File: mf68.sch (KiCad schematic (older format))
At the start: 2 parts, among them SW1 MX, U1 nice_nano

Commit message: Start working on matrix
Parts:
- removed SW1: MX, Keebio-Parts:MX-Alps-Choc-1U, symbol keebio:MX
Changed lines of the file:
@@
 $Descr A4 11693 8268
 encoding utf-8
-Sheet 1 1
+Sheet 1 2
 Title ""
 Date ""
@@
 	1    0    0    -1
 $EndComp
-$Comp
-L keebio:MX SW1
-U 1 1 6192757C
-P 3650 2550
-F 0 "SW1" H 3650 2773 50  0000 C CNN
-F 1 "MX" H 3650 2250 60  0001 C CNN
-F 2 "Keebio-Parts:MX-Alps-Choc-1U" H 3650 2550 60  0001 C CNN
-F 3 "" H 3650 2550 60  0001 C CNN
-	1    3650 2550
-	1    0    0    -1
-$EndComp
+$Sheet
+S 3950 2050 2750 1350
+U 6194AF7C
+F0 "matrix" 50
+F1 "matrix.sch" 50
+$EndSheet
 $EndSCHEMATC

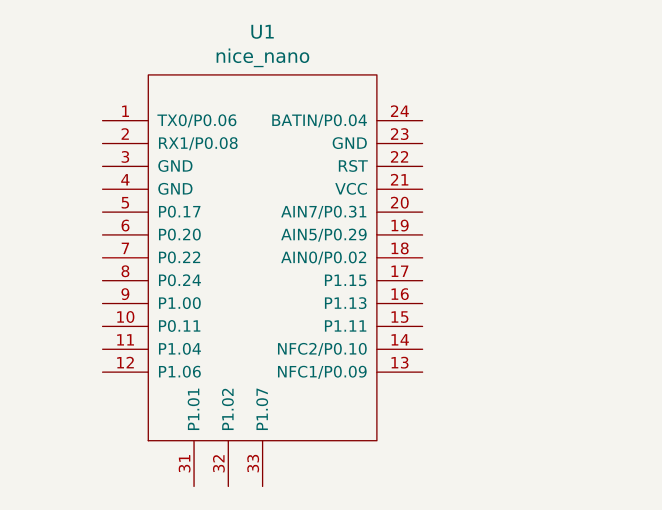
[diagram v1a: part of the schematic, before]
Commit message: Arranged a large amount of switches
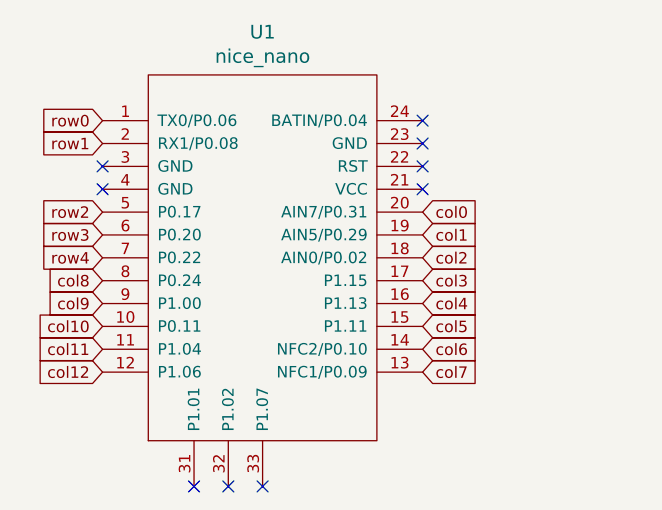
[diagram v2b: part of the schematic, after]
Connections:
- net row0: now reaches U1.1 (TX0/P0.06)
- net col10: now reaches U1.10 (P0.11)
- net col11: now reaches U1.11 (P1.04)
- net col12: now reaches U1.12 (P1.06)
- net col7: now reaches U1.13 (NFC1/P0.09)
- net col6: now reaches U1.14 (NFC2/P0.10)
- net col5: now reaches U1.15 (P1.11)
- net col4: now reaches U1.16 (P1.13)
- net col3: now reaches U1.17 (P1.15)
- net col2: now reaches U1.18 (AIN0/P0.02)
- net col1: now reaches U1.19 (AIN5/P0.29)
- net row1: now reaches U1.2 (RX1/P0.08)
- net col0: now reaches U1.20 (AIN7/P0.31)
- net row2: now reaches U1.5 (P0.17)
- net row3: now reaches U1.6 (P0.20)
- net row4: now reaches U1.7 (P0.22)
- net col8: now reaches U1.8 (P0.24)
- net col9: now reaches U1.9 (P1.00)
- no-connect marks 0 -> 9
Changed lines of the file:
@@
 F1 "matrix.sch" 50
 $EndSheet
+Text GLabel 1450 2350 0    50   Input ~ 0
+row0
+Text GLabel 1450 2450 0    50   Input ~ 0
+row1
+Text GLabel 1450 2750 0    50   Input ~ 0
+row2
+Text GLabel 1450 2850 0    50   Input ~ 0
+row3
+Text GLabel 1450 2950 0    50   Input ~ 0
+row4
+Text GLabel 2850 2750 2    50   Input ~ 0
+col0
+Text GLabel 2850 2850 2    50   Input ~ 0
+col1
+Text GLabel 2850 2950 2    50   Input ~ 0
+col2
+Text GLabel 2850 3050 2    50   Input ~ 0
+col3
+Text GLabel 2850 3150 2    50   Input ~ 0
+col4
+Text GLabel 2850 3250 2    50   Input ~ 0
+col5
+Text GLabel 2850 3350 2    50   Input ~ 0
+col6
+Text GLabel 2850 3450 2    50   Input ~ 0
+col7
+NoConn ~ 1450 2550
+NoConn ~ 1450 2650
+NoConn ~ 2850 2450
+NoConn ~ 2850 2550
+NoConn ~ 2850 2650
+NoConn ~ 2850 2350
+NoConn ~ 2150 3950
+NoConn ~ 2000 3950
+NoConn ~ 1850 3950
+Text GLabel 1450 3450 0    50   Input ~ 0
+col12
+Text GLabel 1450 3350 0    50   Input ~ 0
+col11
+Text GLabel 1450 3250 0    50   Input ~ 0
+col10
+Text GLabel 1450 3150 0    50   Input ~ 0
+col9
+Text GLabel 1450 3050 0    50   Input ~ 0
+col8
 $EndSCHEMATC

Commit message: Wip: row stagger is wrong!
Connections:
- net col0: now also U1.19 (AIN5/P0.29); no longer U1.20 (AIN7/P0.31)
- net col1: now also U1.18 (AIN0/P0.02); no longer U1.19 (AIN5/P0.29)
- net col10: now also U1.8 (P0.24); no longer U1.10 (P0.11)
- net col12: now also U1.10 (P0.11); no longer U1.12 (P1.06)
- net col2: now also U1.17 (P1.15); no longer U1.18 (AIN0/P0.02)
- net col3: now also U1.16 (P1.13); no longer U1.17 (P1.15)
- net col4: now also U1.15 (P1.11); no longer U1.16 (P1.13)
- net col5: now also U1.14 (NFC2/P0.10); no longer U1.15 (P1.11)
- net col6: now also U1.13 (NFC1/P0.09); no longer U1.14 (NFC2/P0.10)
- net col7: now also U1.2 (RX1/P0.08); no longer U1.13 (NFC1/P0.09)
- net col8: now also U1.6 (P0.20); no longer U1.8 (P0.24)
- net col9: now also U1.7 (P0.22); no longer U1.9 (P1.00)
- net row0: now also U1.20 (AIN7/P0.31); no longer U1.1 (TX0/P0.06)
- net row1: now also U1.1 (TX0/P0.06); no longer U1.2 (RX1/P0.08)
- net row3: now also U1.12 (P1.06); no longer U1.6 (P0.20)
- net row4: now also U1.9 (P1.00); no longer U1.7 (P0.22)
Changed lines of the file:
@@
 $EndSheet
 Text GLabel 1450 2350 0    50   Input ~ 0
-row0
-Text GLabel 1450 2450 0    50   Input ~ 0
 row1
 Text GLabel 1450 2750 0    50   Input ~ 0
 row2
-Text GLabel 1450 2850 0    50   Input ~ 0
+Text GLabel 1450 3450 0    50   Input ~ 0
 row3
-Text GLabel 1450 2950 0    50   Input ~ 0
+Text GLabel 1450 3150 0    50   Input ~ 0
 row4
-Text GLabel 2850 2750 2    50   Input ~ 0
+Text GLabel 2850 2850 2    50   Input ~ 0
 col0
-Text GLabel 2850 2850 2    50   Input ~ 0
+Text GLabel 2850 2950 2    50   Input ~ 0
 col1
-Text GLabel 2850 2950 2    50   Input ~ 0
+Text GLabel 2850 3050 2    50   Input ~ 0
 col2
-Text GLabel 2850 3050 2    50   Input ~ 0
+Text GLabel 2850 3150 2    50   Input ~ 0
 col3
-Text GLabel 2850 3150 2    50   Input ~ 0
-col4
-Text GLabel 2850 3250 2    50   Input ~ 0
-col5
-Text GLabel 2850 3350 2    50   Input ~ 0
-col6
-Text GLabel 2850 3450 2    50   Input ~ 0
+Text GLabel 1450 2450 0    50   Input ~ 0
 col7
 NoConn ~ 1450 2550
@@
 NoConn ~ 2000 3950
 NoConn ~ 1850 3950
-Text GLabel 1450 3450 0    50   Input ~ 0
+Text GLabel 1450 3250 0    50   Input ~ 0
 col12
 Text GLabel 1450 3350 0    50   Input ~ 0
 col11
-Text GLabel 1450 3250 0    50   Input ~ 0
+Text GLabel 1450 3050 0    50   Input ~ 0
 col10
-Text GLabel 1450 3150 0    50   Input ~ 0
+Text GLabel 1450 2950 0    50   Input ~ 0
 col9
-Text GLabel 1450 3050 0    50   Input ~ 0
+Text GLabel 1450 2850 0    50   Input ~ 0
 col8
+Text GLabel 2850 2750 2    50   Input ~ 0
+row0
+Text GLabel 2850 3250 2    50   Input ~ 0
+col4
+Text GLabel 2850 3450 2    50   Input ~ 0
+col6
+Text GLabel 2850 3350 2    50   Input ~ 0
+col5
 $EndSCHEMATC

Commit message: Fixed annotations, Only missing battery dip switch
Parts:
- added POWER_SW1: SW_SPDT, Button_Switch_THT:SW_E-Switch_EG1224_SPDT_Angled, symbol Switch:SW_SPDT
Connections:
- net at U1.23 (GND): now also POWER_SW1.2 (B), POWER_SW1.3 (C)
- net at U1.24 (BATIN/P0.04): now also POWER_SW1.1 (A)
- no-connect marks 9 -> 7
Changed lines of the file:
@@
 Comment4 ""
 $EndDescr
-$Comp
-L nice_nano:nice_nano U1
-U 1 1 61924FB8
-P 2150 2900
-F 0 "U1" H 2150 3837 60  0000 C CNN
-F 1 "nice_nano" H 2150 3731 60  0000 C CNN
-F 2 "nice-nano-kicad:nice_nano" V 3200 400 60  0001 C CNN
-F 3 "" V 3200 400 60  0001 C CNN
-	1    2150 2900
-	1    0    0    -1
-$EndComp
 $Sheet
 S 3950 2050 2750 1350
@@
 Text GLabel 1450 2450 0    50   Input ~ 0
 col7
-NoConn ~ 1450 2550
 NoConn ~ 1450 2650
-NoConn ~ 2850 2450
 NoConn ~ 2850 2550
-NoConn ~ 2850 2650
-NoConn ~ 2850 2350
 NoConn ~ 2150 3950
 NoConn ~ 2000 3950
@@
 Text GLabel 2850 3350 2    50   Input ~ 0
 col5
+NoConn ~ 1450 2550
+$Comp
+L nice_nano:nice_nano U1
+U 1 1 61924FB8
+P 2150 2900
+F 0 "U1" H 2150 3837 60  0000 C CNN
+F 1 "nice_nano" H 2150 3731 60  0000 C CNN
+F 2 "nice-nano-kicad:nice_nano" V 3200 400 60  0001 C CNN
+F 3 "" V 3200 400 60  0001 C CNN
+	1    2150 2900
+	1    0    0    -1
+$EndComp
+Wire Wire Line
+	2850 2450 3350 2450
+Wire Wire Line
+	3450 3950 3450 4150
+Wire Wire Line
+	3350 2450 3350 3500
+$Comp
+L Switch:SW_SPDT POWER_SW1
+U 1 1 619FA1F3
+P 3350 3750
+F 0 "POWER_SW1" V 3350 3898 50  0000 L CNN
+F 1 "SW_SPDT" H 3350 3944 50  0001 C CNN
+F 2 "Button_Switch_THT:SW_E-Switch_EG1224_SPDT_Angled" H 3350 3750 50  0001 C CNN
+F 3 "~" H 3350 3750 50  0001 C CNN
+	1    3350 3750
+	0    1    1    0
+$EndComp
+Wire Wire Line
+	3250 3950 3250 4150
+Wire Wire Line
+	3250 4150 3100 4150
+Wire Wire Line
+	3100 4150 3100 3500
+Wire Wire Line
+	3100 3500 3350 3500
+Connection ~ 3350 3500
+Wire Wire Line
+	3350 3500 3350 3550
+Wire Wire Line
+	3450 4150 3800 4150
+Wire Wire Line
+	3800 4150 3800 2350
+Wire Wire Line
+	3800 2350 2850 2350
+NoConn ~ 2850 2650
 $EndSCHEMATC

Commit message: new: Add footprint for microswitch and battery
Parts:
- added BT1: Battery, Connector_PinSocket_2.54mm:PinSocket_1x02_P2.54mm_Vertical, symbol Device:Battery_Cell
- POWER_SW1: footprint Button_Switch_THT:SW_E-Switch_EG1224_SPDT_Angled -> xeal_components:SS12D00
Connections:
- net at POWER_SW1.2 (B), U1.23 (GND): now also POWER_SW1.1 (A); no longer POWER_SW1.3 (C)
- net at U1.24 (BATIN/P0.04): now also BT1.1 (+); no longer POWER_SW1.1 (A)
- new net: BT1.2 (-), POWER_SW1.3 (C)
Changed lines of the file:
@@
 $EndDescr
 $Sheet
-S 3950 2050 2750 1350
+S 4500 1750 2750 1350
 U 6194AF7C
 F0 "matrix" 50
@@
 U 1 1 619FA1F3
 P 3350 3750
-F 0 "POWER_SW1" V 3350 3898 50  0000 L CNN
+F 0 "POWER_SW1" V 3350 3898 50  0000 C TNN
 F 1 "SW_SPDT" H 3350 3944 50  0001 C CNN
-F 2 "Button_Switch_THT:SW_E-Switch_EG1224_SPDT_Angled" H 3350 3750 50  0001 C CNN
+F 2 "xeal_components:SS12D00" H 3350 3750 50  0001 C CNN
 F 3 "~" H 3350 3750 50  0001 C CNN
 	1    3350 3750
-	0    1    1    0
+	0    -1   1    0
 $EndComp
 Wire Wire Line
@@
 	3350 3500 3350 3550
 Wire Wire Line
-	3450 4150 3800 4150
+	3450 4150 3600 4150
 Wire Wire Line
-	3800 4150 3800 2350
+	3600 4150 3600 3550
+NoConn ~ 2850 2650
+$Comp
+L Device:Battery_Cell BT1
+U 1 1 61977CAB
+P 3600 3450
+F 0 "BT1" H 3718 3546 50  0000 L CNN
+F 1 "Battery" H 3718 3455 50  0000 L CNN
+F 2 "Connector_PinSocket_2.54mm:PinSocket_1x02_P2.54mm_Vertical" V 3600 3510 50  0001 C CNN
+F 3 "~" V 3600 3510 50  0001 C CNN
+	1    3600 3450
+	1    0    0    -1
+$EndComp
 Wire Wire Line
-	3800 2350 2850 2350
-NoConn ~ 2850 2650
+	3600 3250 3600 2350
+Wire Wire Line
+	3600 2350 2850 2350
 $EndSCHEMATC

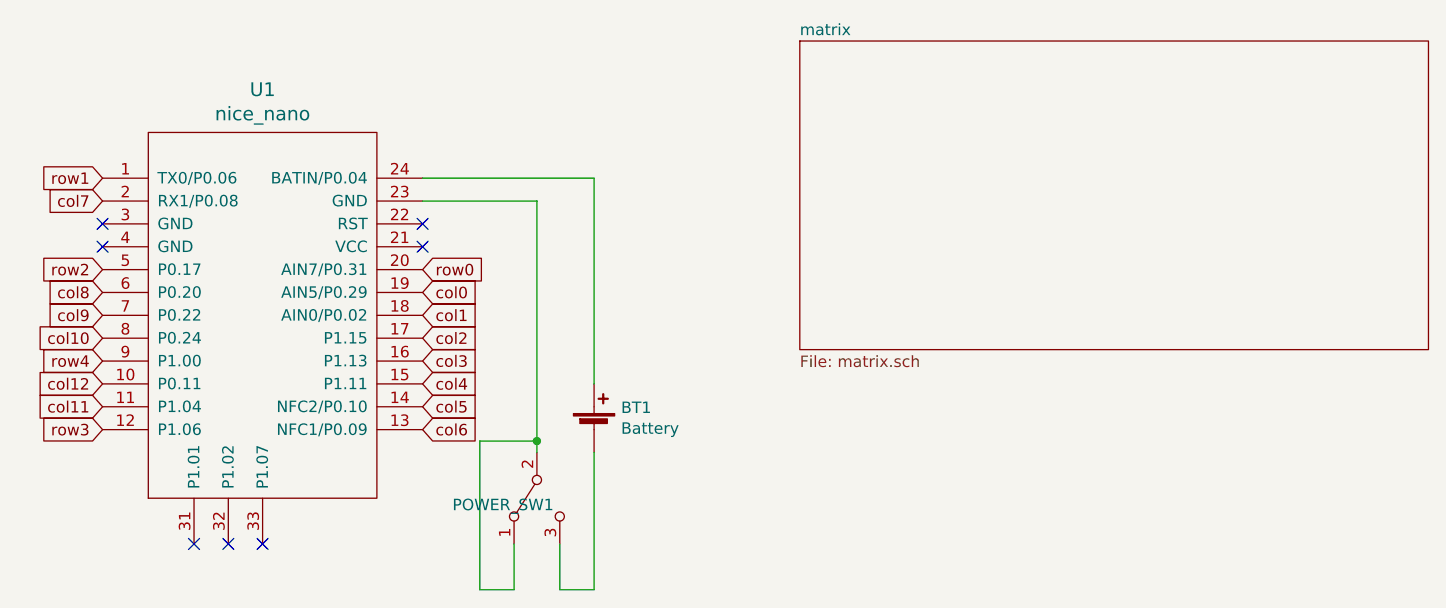
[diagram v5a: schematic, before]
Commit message: Fully connected PCB
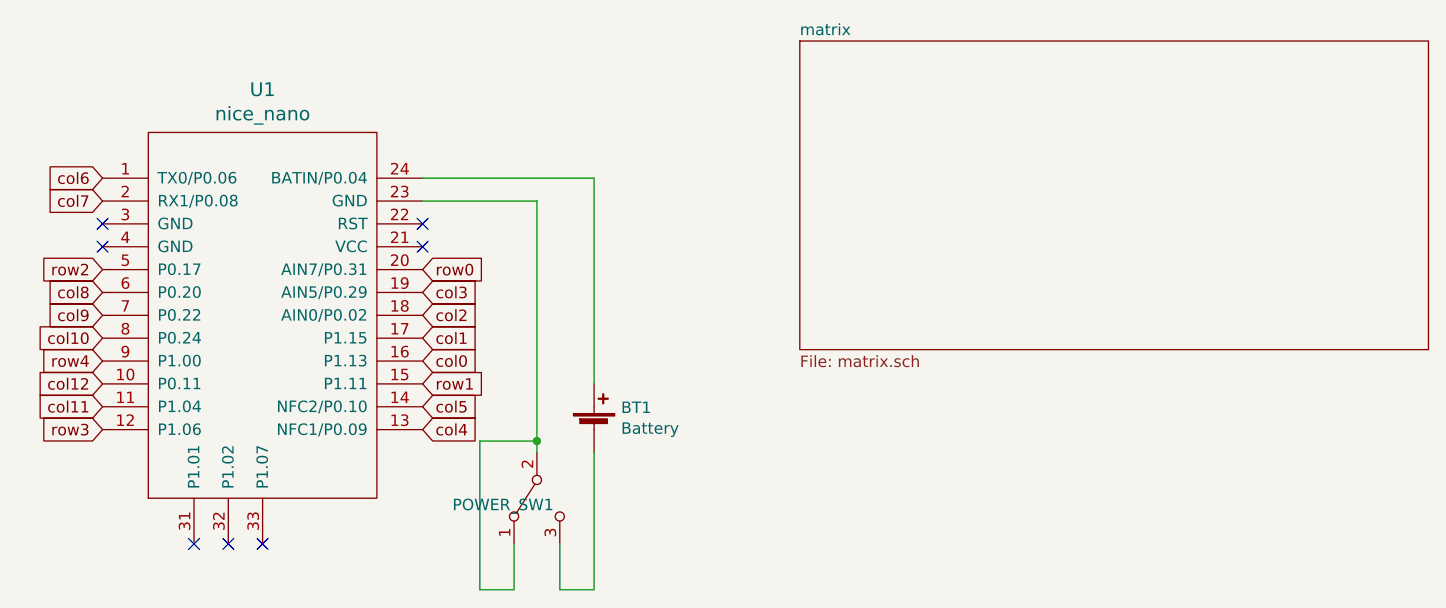
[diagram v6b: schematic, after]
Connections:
- net col0: now also U1.16 (P1.13); no longer U1.19 (AIN5/P0.29)
- net col1: now also U1.17 (P1.15); no longer U1.18 (AIN0/P0.02)
- net col2: now also U1.18 (AIN0/P0.02); no longer U1.17 (P1.15)
- net col3: now also U1.19 (AIN5/P0.29); no longer U1.16 (P1.13)
- net col4: now also U1.13 (NFC1/P0.09); no longer U1.15 (P1.11)
- net col6: now also U1.1 (TX0/P0.06); no longer U1.13 (NFC1/P0.09)
- net row1: now also U1.15 (P1.11); no longer U1.1 (TX0/P0.06)
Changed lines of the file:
@@
 F1 "matrix.sch" 50
 $EndSheet
-Text GLabel 1450 2350 0    50   Input ~ 0
+Text GLabel 2850 3250 2    50   Input ~ 0
 row1
 Text GLabel 1450 2750 0    50   Input ~ 0
@@
 Text GLabel 1450 3150 0    50   Input ~ 0
 row4
+Text GLabel 2850 3150 2    50   Input ~ 0
+col0
+Text GLabel 2850 3050 2    50   Input ~ 0
+col1
+Text GLabel 2850 2950 2    50   Input ~ 0
+col2
 Text GLabel 2850 2850 2    50   Input ~ 0
-col0
-Text GLabel 2850 2950 2    50   Input ~ 0
-col1
-Text GLabel 2850 3050 2    50   Input ~ 0
-col2
-Text GLabel 2850 3150 2    50   Input ~ 0
 col3
 Text GLabel 1450 2450 0    50   Input ~ 0
@@
 Text GLabel 2850 2750 2    50   Input ~ 0
 row0
-Text GLabel 2850 3250 2    50   Input ~ 0
+Text GLabel 2850 3450 2    50   Input ~ 0
 col4
-Text GLabel 2850 3450 2    50   Input ~ 0
+Text GLabel 1450 2350 0    50   Input ~ 0
 col6
 Text GLabel 2850 3350 2    50   Input ~ 0
